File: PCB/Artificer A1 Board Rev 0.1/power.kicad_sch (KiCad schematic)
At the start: 3 parts, among them U2 AXP717, U5 GT-USB-7010ASV, U6 GT-USB-7010ASV

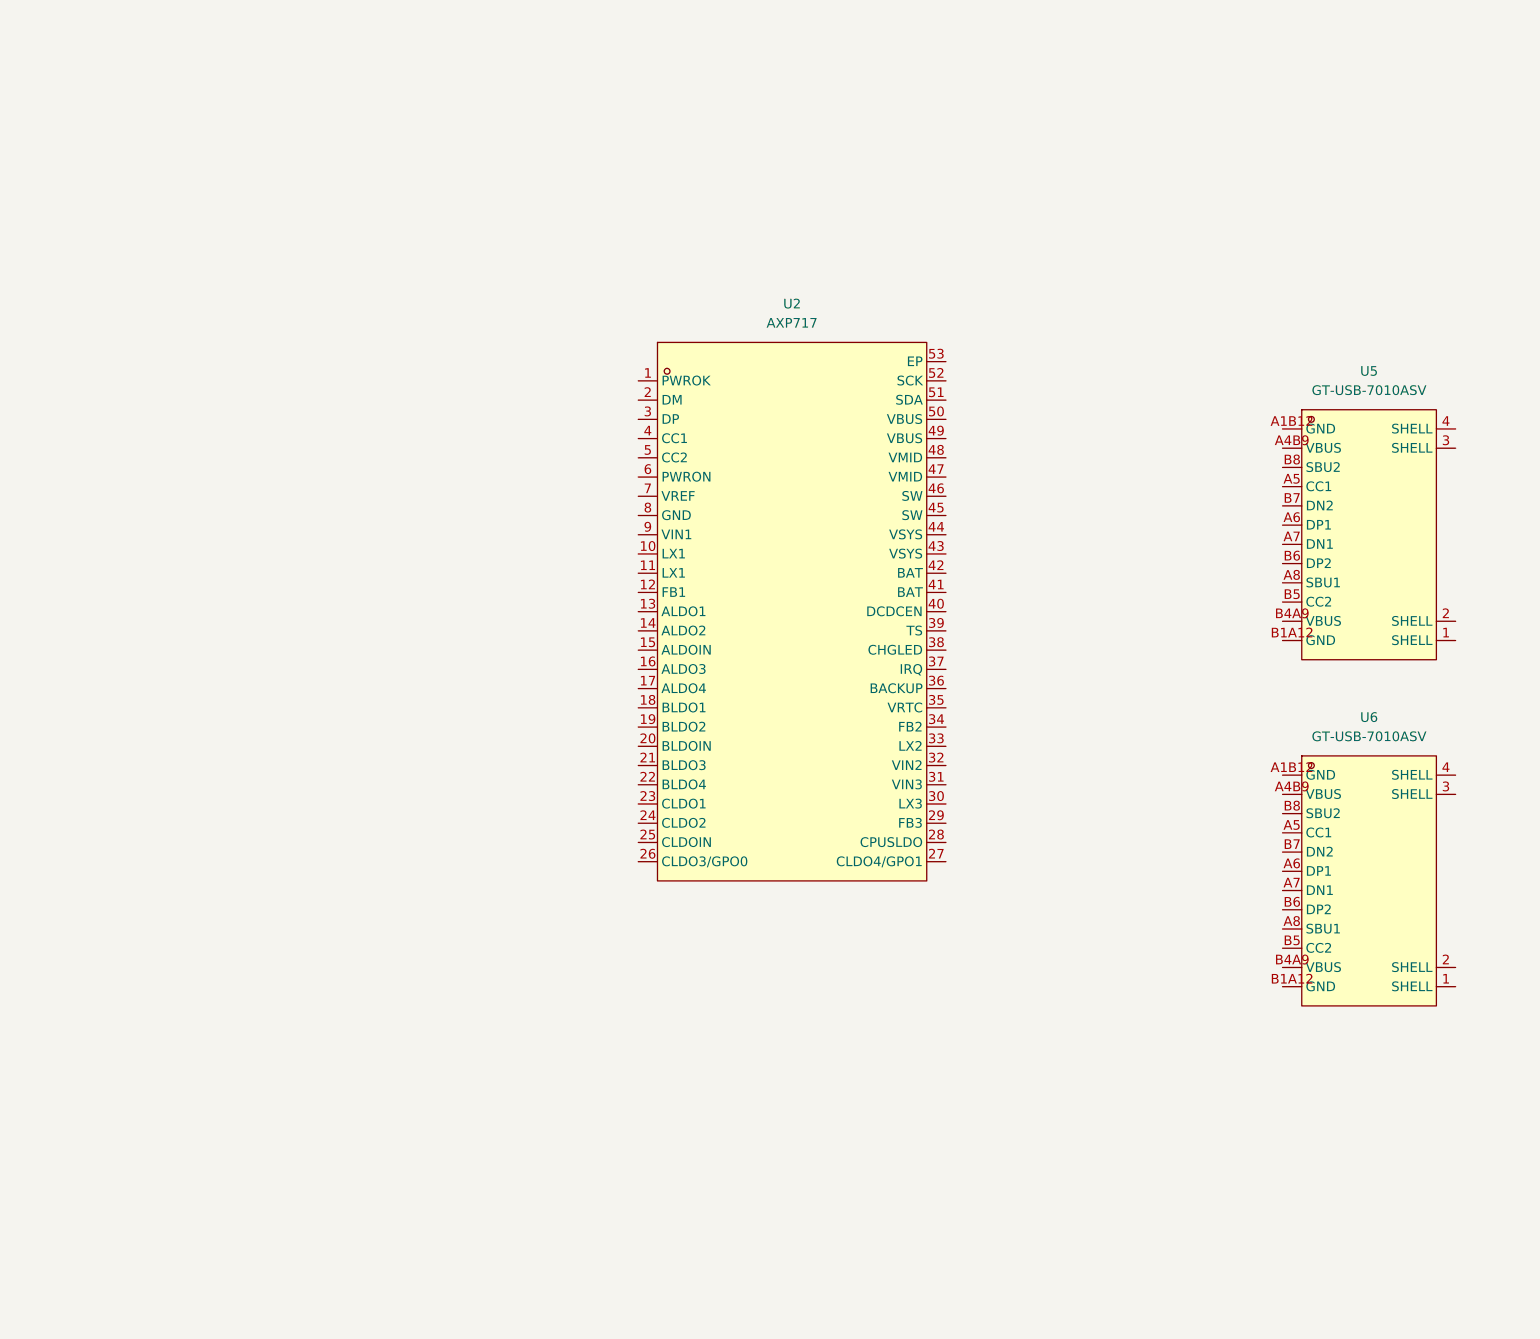
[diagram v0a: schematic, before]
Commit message: schematic update
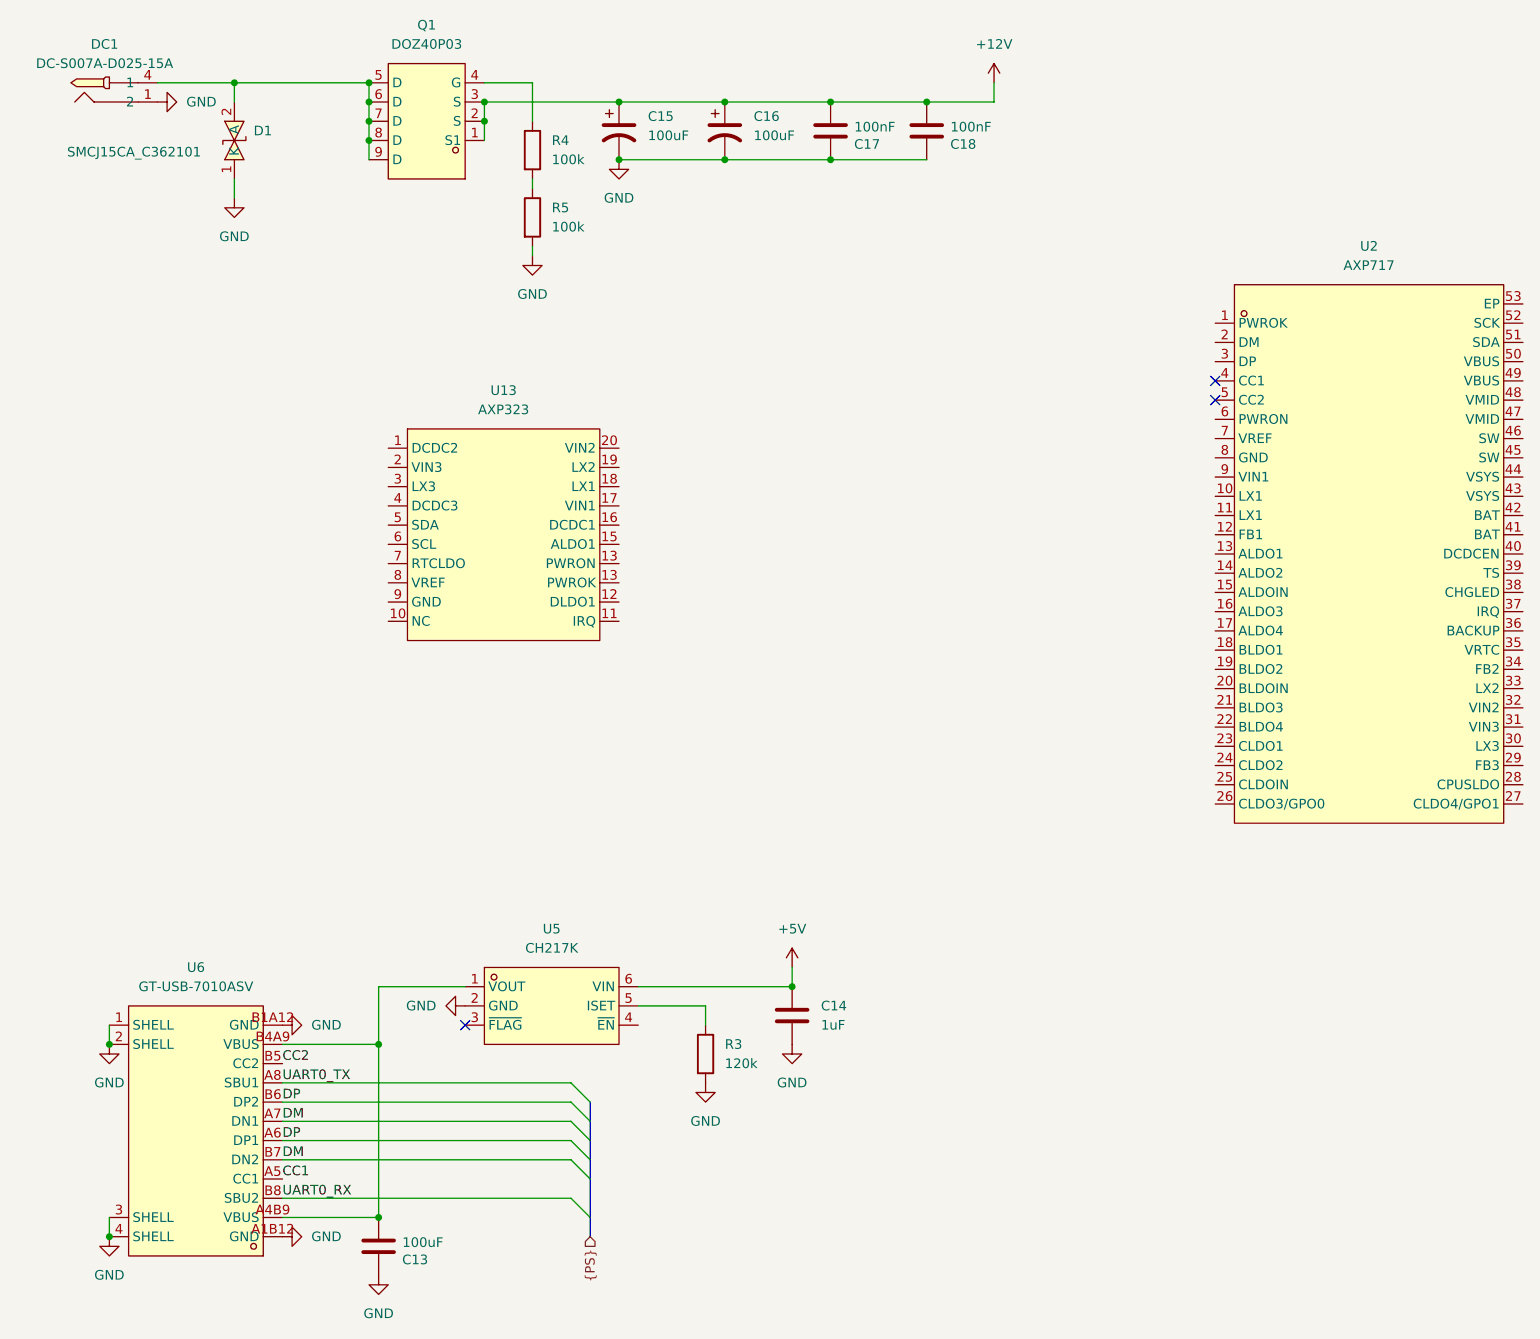
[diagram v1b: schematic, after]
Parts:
- removed U5: GT-USB-7010ASV, easyeda2kicad:USB-C-SMD_G-SWITCH_GT-USB-7010ASV, symbol easyeda2kicad:GT-USB-7010ASV
- added C13: 100uF, symbol Device:C
- added C14: 1uF, symbol Device:C
- added C15, C16: 100uF, symbol Device:C_Polarized_US
- added C17, C18: 100nF, symbol Device:C
- added D1: SMCJ15CA_C362101, easyeda2kicad:SMC_L6.9-W5.9-LS7.9-BI, symbol easyeda2kicad:SMCJ15CA_C362101
- added DC1: DC-S007A-D025-15A, easyeda2kicad:DC-IN-TH_DC-S007A-D020-15A, symbol easyeda2kicad:DC-S007A-D025-15A
- added Q1: DOZ40P03, easyeda2kicad:DFN-8_L3.0-W3.0-P0.65-BL, symbol easyeda2kicad:DOZ40P03
- added R3: 120k, symbol Device:R
- added R4, R5: 100k, symbol Device:R
- added U13: AXP323, local_footprints:AXP323, symbol AXP323:AXP323
- added U5: CH217K, easyeda2kicad:SOT-23-6_L2.9-W1.6-P0.95-LS2.8-BL, symbol easyeda2kicad:CH217K
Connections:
- net GND: now reaches U6.1 (SHELL)
- net GND: now also U6.2 (SHELL), U6.3 (SHELL), U6.4 (SHELL), U6.A1B12 (GND), U6.B1A12 (GND), C13.1, C14.1, C15.2, C16.2, C17.1, C18.1, D1.1 (K), DC1.1 (2), R3.2, R5.2, U5.2 (GND)
- net at U6.A4B9 (VBUS): now also U6.B4A9 (VBUS), C13.2, U5.1 (VOUT)
- net CC1: now reaches U6.A5 (CC1)
- net DP: now reaches U6.A6 (DP1)
- net DP: now also U6.B6 (DP2)
- net DM: now reaches U6.A7 (DN1)
- net DM: now also U6.B7 (DN2)
- net UART0_TX: now reaches U6.A8 (SBU1)
- net CC2: now reaches U6.B5 (CC2)
- net UART0_RX: now reaches U6.B8 (SBU2)
- new net: D1.2 (A), DC1.4 (1), Q1.5 (D), Q1.6 (D), Q1.7 (D), Q1.8 (D), Q1.9 (D)
- new net: R4.2, R5.1
- new net: R3.1, U5.5 (ISET)
- new net: Q1.4 (G), R4.1
- new net +12V: C15.1, C16.1, C17.2, C18.2, Q1.1 (S1), Q1.2 (S), Q1.3 (S)
- new net +5V: C14.2, U5.6 (VIN)
- no-connect marks 0 -> 3
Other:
- moved on the sheet: U2, U6

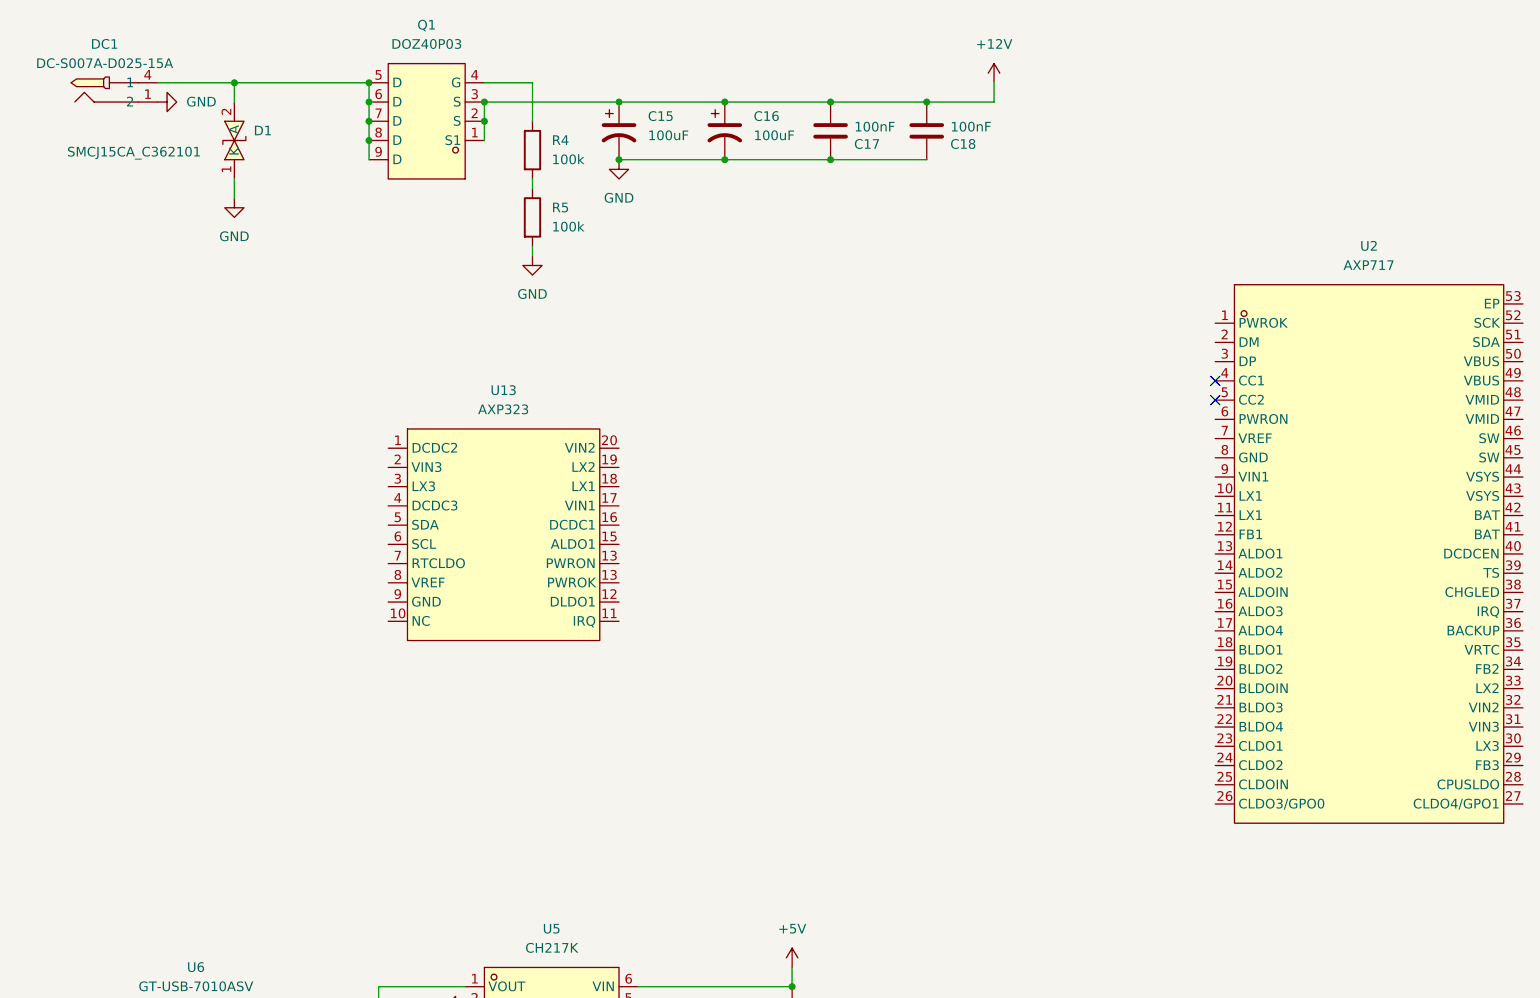
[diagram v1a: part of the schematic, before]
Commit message: localized libraries
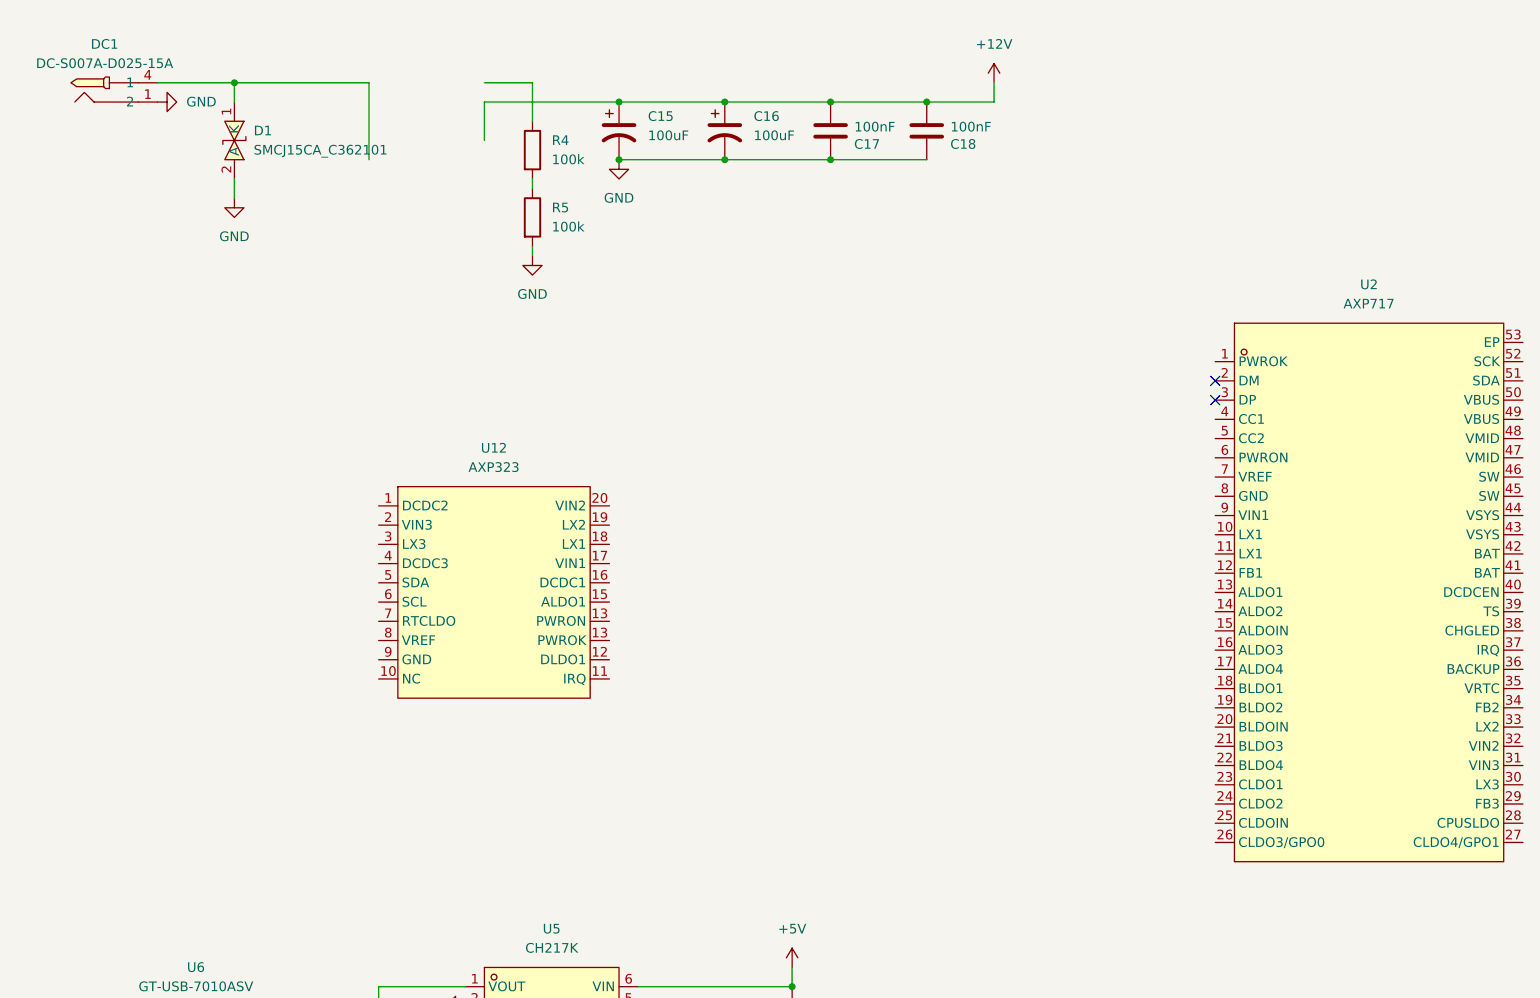
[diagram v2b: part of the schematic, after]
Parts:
- removed D1: SMCJ15CA_C362101, easyeda2kicad:SMC_L6.9-W5.9-LS7.9-BI, symbol easyeda2kicad:SMCJ15CA_C362101
- removed DC1: DC-S007A-D025-15A, easyeda2kicad:DC-IN-TH_DC-S007A-D020-15A, symbol easyeda2kicad:DC-S007A-D025-15A
- removed Q1: DOZ40P03, easyeda2kicad:DFN-8_L3.0-W3.0-P0.65-BL, symbol easyeda2kicad:DOZ40P03
- removed U13: AXP323, local_footprints:AXP323, symbol AXP323:AXP323
- removed U2: AXP717, easyeda2kicad:QFN-52_L6.0-W6.0-P0.40-TL-EP4.7, symbol easyeda2kicad:AXP717
- removed U5: CH217K, easyeda2kicad:SOT-23-6_L2.9-W1.6-P0.95-LS2.8-BL, symbol easyeda2kicad:CH217K
- removed U6: GT-USB-7010ASV, easyeda2kicad:USB-C-SMD_G-SWITCH_GT-USB-7010ASV, symbol easyeda2kicad:GT-USB-7010ASV
- added D1: SMCJ15CA_C362101, easyeda:SMC_L6.9-W5.9-LS7.9-BI, symbol easyeda:SMCJ15CA_C362101
- added DC1: DC-S007A-D025-15A, easyeda:DC-IN-TH_DC-S007A-D020-15A, symbol easyeda:DC-S007A-D025-15A
- added U12: AXP323, custom footprints:AXP323, symbol AXP323:AXP323
- added U2: AXP717, easyeda:QFN-52_L6.0-W6.0-P0.40-TL-EP4.7, symbol easyeda:AXP717
- added U5: CH217K, easyeda:SOT-23-6_L2.9-W1.6-P0.95-LS2.8-BL, symbol easyeda:CH217K
- added U6: GT-USB-7010ASV, easyeda:USB-C-SMD_G-SWITCH_GT-USB-7010ASV, symbol easyeda:GT-USB-7010ASV
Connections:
- net +5V: now also U5.6 (VIN)
- net CC1: now also U6.A5 (CC1)
- net CC2: now also U6.B5 (CC2)
- net DM: now also U6.A7 (DN1), U6.B7 (DN2)
- net DP: now also U6.A6 (DP1), U6.B6 (DP2)
- net GND: now also D1.2 (A), DC1.1 (2), U5.2 (GND), U6.1 (SHELL), U6.2 (SHELL), U6.3 (SHELL), U6.4 (SHELL), U6.A1B12 (GND), U6.B1A12 (GND)
- net UART0_RX: now also U6.B8 (SBU2)
- net UART0_TX: now also U6.A8 (SBU1)
- net at C13.2: now also U5.1 (VOUT), U6.A4B9 (VBUS), U6.B4A9 (VBUS)
- net at R3.1: now also U5.5 (ISET)
- new net: D1.1 (K), DC1.4 (1)
